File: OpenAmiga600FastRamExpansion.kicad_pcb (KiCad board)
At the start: 2 copper layers, 71.8 x 72 mm, 11 parts, among them J1 MC68000_PLCC68, P1 JTAG_CONNECTOR, P99 OSHW_LOGO, U1 ATF1502AS-10JU44, U2 74LS157, U3 HYB5118160BSJ, U4 HYB5118160BSJ, U7 74LS157

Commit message: Ready for routing!
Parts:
- removed U7: 74LS157, Package_SO:SOIC-16W_5.3x10.2mm_P1.27mm
- added C1: 100n, Capacitor_SMD:C_0805_2012Metric_Pad1.15x1.40mm_HandSolder, F.Cu at (168.4, 77.2)
- added C10: 100n, Capacitor_SMD:C_0805_2012Metric_Pad1.15x1.40mm_HandSolder, B.Cu at (150.5, 112.3)
- added C11: 100n, Capacitor_SMD:C_0805_2012Metric_Pad1.15x1.40mm_HandSolder, B.Cu at (162.2, 113.3)
- added C12: 100n, Capacitor_SMD:C_0805_2012Metric_Pad1.15x1.40mm_HandSolder, B.Cu at (173.6, 109.3)
- added C13: 100n, Capacitor_SMD:CP_Elec_5x5.8, F.Cu at (157.3, 90.8)
- added C14: 100n, Capacitor_SMD:CP_Elec_5x5.8, F.Cu at (157.3, 77.1)
- added C2: 100n, Capacitor_SMD:C_0805_2012Metric_Pad1.15x1.40mm_HandSolder, F.Cu at (165.6, 90.2)
- added C3: 100n, Capacitor_SMD:C_0805_2012Metric_Pad1.15x1.40mm_HandSolder, F.Cu at (124.0, 62.2)
- added C4: 100n, Capacitor_SMD:C_0805_2012Metric_Pad1.15x1.40mm_HandSolder, B.Cu at (133.3, 62.2)
- added C5: 100n, Capacitor_SMD:C_0805_2012Metric_Pad1.15x1.40mm_HandSolder, B.Cu at (152.4, 62.2)
- added C6: 100n, Capacitor_SMD:C_0805_2012Metric_Pad1.15x1.40mm_HandSolder, F.Cu at (124.0, 78.7)
- added C7: 100n, Capacitor_SMD:C_0805_2012Metric_Pad1.15x1.40mm_HandSolder, B.Cu at (133.3, 78.7)
- added C8: 100n, Capacitor_SMD:C_0805_2012Metric_Pad1.15x1.40mm_HandSolder, B.Cu at (152.4, 78.7)
- added C9: 100n, Capacitor_SMD:C_0805_2012Metric_Pad1.15x1.40mm_HandSolder, B.Cu at (162.3, 105.7)
- added LD1: LED, OpenAmiga600FastRamExpansion:LED_0805_HandSoldering_ModSilkS, F.Cu at (114.9, 96.8)
- added P98: SCREW_HOLE, MountingHole:MountingHole_2.5mm, F.Cu at (114.0, 102.0)
- added R4: 10k, Resistor_SMD:R_0805_2012Metric_Pad1.15x1.40mm_HandSolder, F.Cu at (114.9, 91.6)
- added U5: ATF1502AS-10JU44, Package_LCC:PLCC-44_THT-Socket, F.Cu at (163.5, 103.1)
- J1: footprint Package_LCC:PLCC-68_THT-Socket -> OpenAmiga600FastRamExpansion:PLCC-68_THT-SocketUpsideDown
- U1: value ATF1502AS-10JU44 -> 74LS157; footprint Package_LCC:PLCC-44_THT-Socket -> Package_SO:SOIC-16_3.9x9.9mm_P1.27mm
- U2: footprint Package_SO:SOIC-16W_5.3x10.2mm_P1.27mm -> Package_SO:SOIC-16_3.9x9.9mm_P1.27mm
- U3, U4: footprint OpenAmiga600FastRamExpansion:SOJ-42-Socket-LongPads -> OpenAmiga600FastRamExpansion:SOJ-42-LongPads
- moved P99 58.5 mm to (116.0, 122.8)
- moved R2 22.1 mm to (178.4, 121.8)
- moved R1 21.0 mm to (178.7, 102.5), turned to 180 degrees
- moved U1 20.4 mm to (175.3, 77.1), turned to 90 degrees
- moved J1 19.4 mm to (132.7, 93.0)
- moved U2 18.2 mm to (172.7, 90.2)
- moved U3 16.9 mm to (139.7, 62.3)
- moved U4 16.4 mm to (139.7, 78.7)
- moved R3 13.1 mm to (178.6, 105.0), turned to 180 degrees
- moved P1 12.7 mm to (177.3, 108.2)
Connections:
- U1 pad 1: /~reset -> /mux_switch
- U1 pad 10: GND -> /a12
- U1 pad 11: /d15 -> /a9
- U1 pad 12: /a23 -> /ma9
- U1 pad 13: /jtag_tms -> /a11
- U1 pad 14: /a22 -> /a10
- U1 pad 15: VCC -> GND
- U1 pad 16: /a21 -> VCC
- U1 pad 2: /~as -> /a7
- U1 pad 3: VCC -> /a14
- U1 pad 4: /ma1 -> /ma6
- U1 pad 5: /ma0 -> /a8
- U1 pad 6: /d12 -> /a13
- U1 pad 7: /jtag_tdi -> /ma7
- U1 pad 8: /d13 -> GND
- U1 pad 9: /d14 -> /ma8
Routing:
- added copper zone on B.Cu, net GND
- added copper zone on F.Cu, net GND
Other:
- outline, holes or cut-outs redrawn
- net class Default: trace_width 0.25 -> 0.2; via_dia 0.8 -> 0.6
- net class Power added: clearance 0.2, trace_width 0.5, via_dia 0.8, via_drill 0.6
- board text added: "JTAG"

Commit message: Final disposition?
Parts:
- moved C1 2.80 mm to (165.6, 77.1)
- moved U1 2.65 mm to (172.7, 77.1)
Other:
- board size 71.8 x 72 mm -> 71.7 x 72 mm

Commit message: Routing in progress...
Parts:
- removed C14: 100n, Capacitor_SMD:CP_Elec_5x5.8
- C13: value 100n -> 10u; footprint Capacitor_SMD:CP_Elec_5x5.8 -> Capacitor_THT:CP_Radial_D5.0mm_P2.00mm
- C5, C8: moved to F.Cu
- moved C13 45.6 mm to (114.3, 106.0)
- moved C5 3.05 mm to (155.4, 62.2)
- moved C8 3.05 mm to (155.4, 78.7)
- moved R2 0.49 mm to (178.6, 121.3), turned to 180 degrees
- moved C9 0.13 mm to (162.2, 105.7)
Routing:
- net /clk: track 0.00 -> 109.3 mm, vias 0 -> 2
- net /~ucas: track 0.00 -> 105.2 mm, vias 0 -> 1
- net /~reset: track 0.00 -> 104.4 mm, vias 0 -> 2
- net /a16: track 0.00 -> 90.2 mm, vias 0 -> 2
- net /d14: track 0.00 -> 80.1 mm, vias 0 -> 1
- net /a8: track 0.00 -> 72.8 mm, vias 0 -> 1
- net /ma8: track 0.00 -> 66.2 mm, vias 0 -> 2
- net /ma9: track 0.00 -> 64.7 mm, vias 0 -> 2
- net /ma7: track 0.00 -> 63.5 mm, vias 0 -> 2
- net VCC: track 0.00 -> 62.4 mm
- net /ma6: track 0.00 -> 57.7 mm, vias 0 -> 2
- net /d13: track 0.00 -> 52.9 mm, vias 0 -> 1
- net /a1: track 0.00 -> 52.8 mm
- net /r~w: track 0.00 -> 52.3 mm
- net /jtag_tms: track 0.00 -> 45.7 mm
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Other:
- outline, holes or cut-outs redrawn
- rule pad_to_mask_clearance: 0.051 -> 0

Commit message: Routing in progress... (Part II)
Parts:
- moved C10 8.73 mm to (159.1, 111.0)
- moved C7 1.02 mm to (132.3, 78.7), turned to 180 degrees
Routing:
- net /~lcas: track 17.0 -> 89.0 mm, vias 0 -> 3
- net /mux_switch: track 0.00 -> 69.1 mm, vias 0 -> 4
- net /a12: track 0.00 -> 68.7 mm, vias 0 -> 1
- net /a10: track 0.00 -> 67.7 mm, vias 0 -> 1
- net /a9: track 0.00 -> 65.9 mm, vias 0 -> 1
- net /~ras2: track 0.00 -> 65.3 mm, vias 0 -> 2
- net /a11: track 0.00 -> 64.6 mm, vias 0 -> 1
- net /a7: track 0.00 -> 57.7 mm, vias 0 -> 1
- net /a13: track 0.00 -> 56.6 mm, vias 0 -> 1
- net /a14: track 0.00 -> 55.1 mm, vias 0 -> 1
- net /a15: track 0.00 -> 49.0 mm, vias 0 -> 1
- net /d12: track 17.0 -> 65.8 mm, vias 0 -> 1
- net /a3: track 40.9 -> 85.9 mm
- net /d15: track 44.0 -> 88.5 mm, vias 0 -> 1
- net /a17: track 21.6 -> 63.8 mm, vias 0 -> 2
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
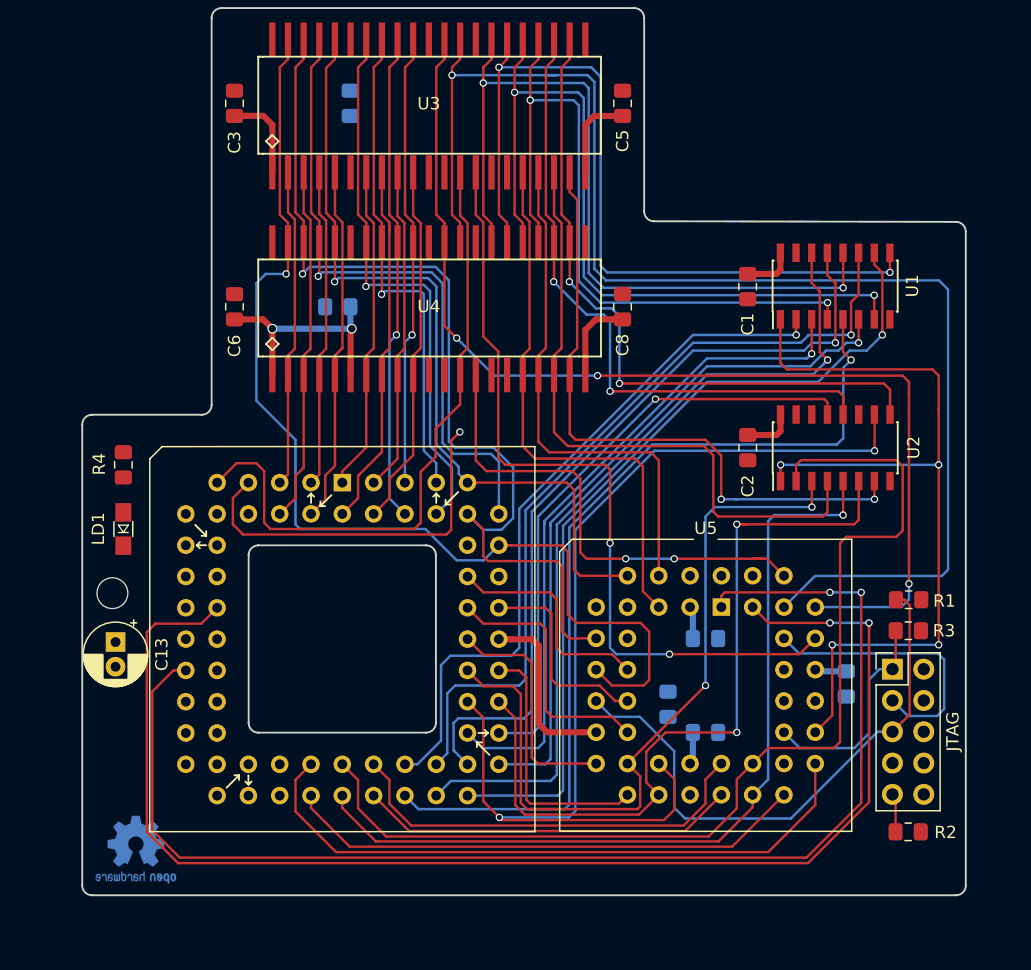
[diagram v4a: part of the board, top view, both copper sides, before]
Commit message: Routing almost done, only power TBD Also added 3D models for all components
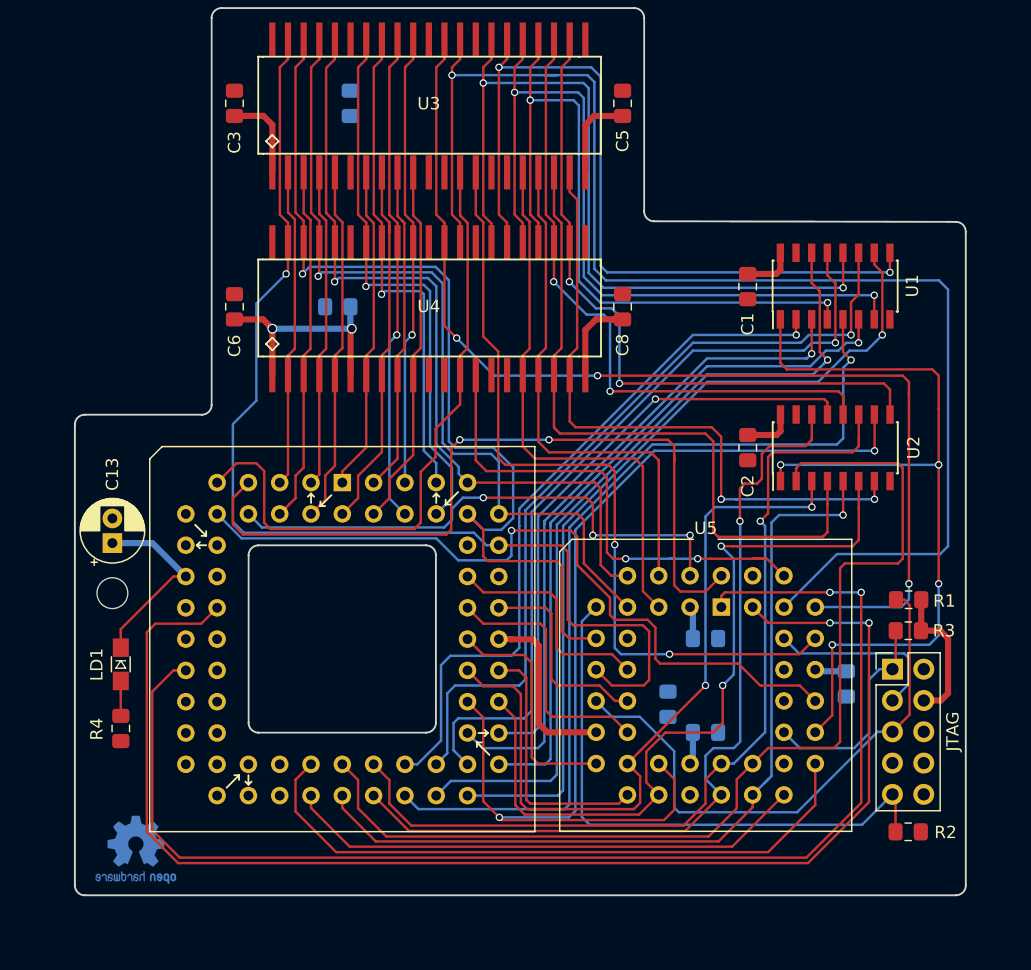
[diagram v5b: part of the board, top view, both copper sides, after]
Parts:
- moved R4 21.4 mm to (114.7, 113.0), turned to 270 degrees
- moved LD1 11.0 mm to (114.7, 107.8), turned to 270 degrees
- moved C13 8.04 mm to (114.0, 97.9), turned to 90 degrees
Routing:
- net /~lds: track 0.00 -> 61.7 mm, vias 0 -> 1
- net /jtag_tdi: track 3.14 -> 47.1 mm
- net /~as: track 0.00 -> 43.9 mm, vias 0 -> 3
- net /a6: track 30.6 -> 68.9 mm, vias 0 -> 1
- net /a5: track 34.6 -> 72.3 mm, vias 0 -> 1
- net /~uds: track 30.3 -> 63.7 mm, vias 1 -> 2
- net VCC: track 71.7 -> 99.0 mm
- net /d13: track 52.8 -> 68.4 mm
- net /jtag_tdo: track 22.7 -> 14.8 mm
- net /ma2: track 51.9 -> 55.7 mm
- net Net-(LD1-Pad2): track 0.00 -> 2.83 mm
- net /d15: track 88.5 -> 91.3 mm
- net /~ucas: track 111.6 -> 110.5 mm
- net /a17: track 63.8 -> 64.8 mm
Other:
- board size 71.7 x 72 mm -> 72.3 x 72 mm

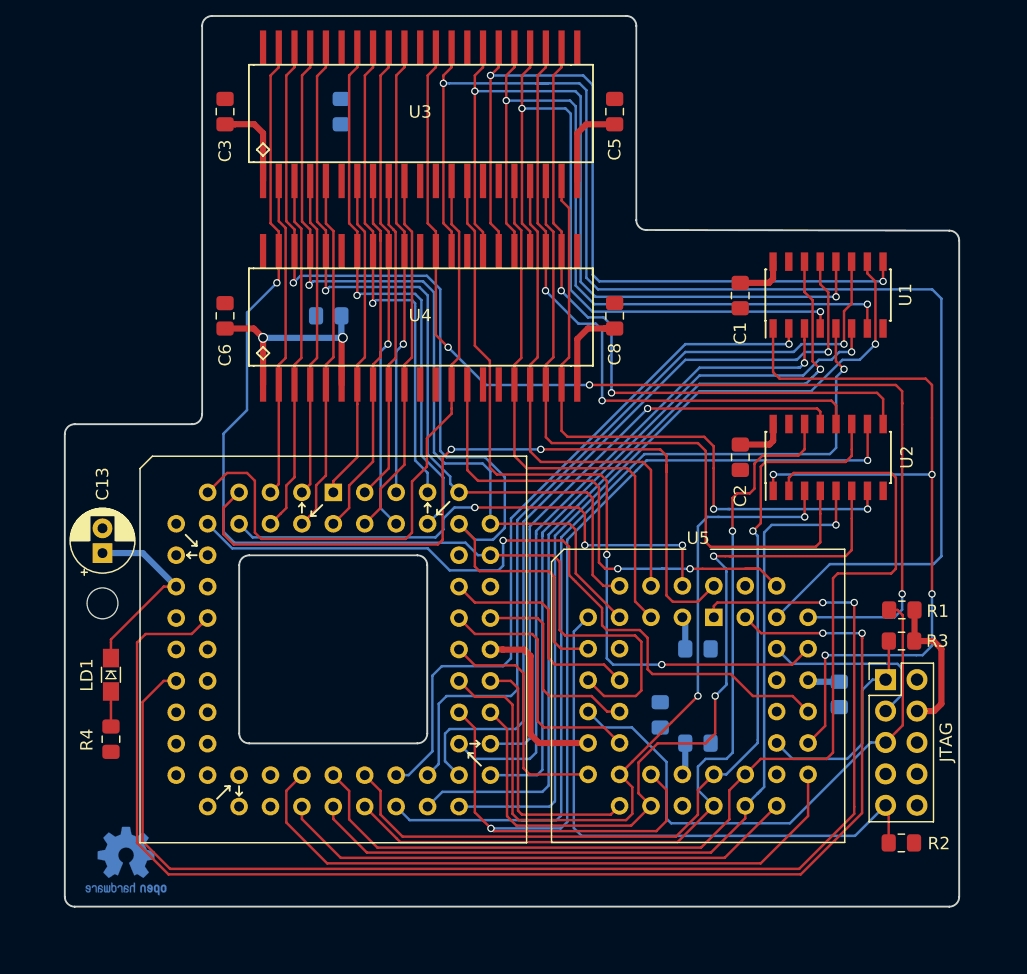
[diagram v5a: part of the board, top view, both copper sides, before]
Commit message: Routing complete Still needs some refinements
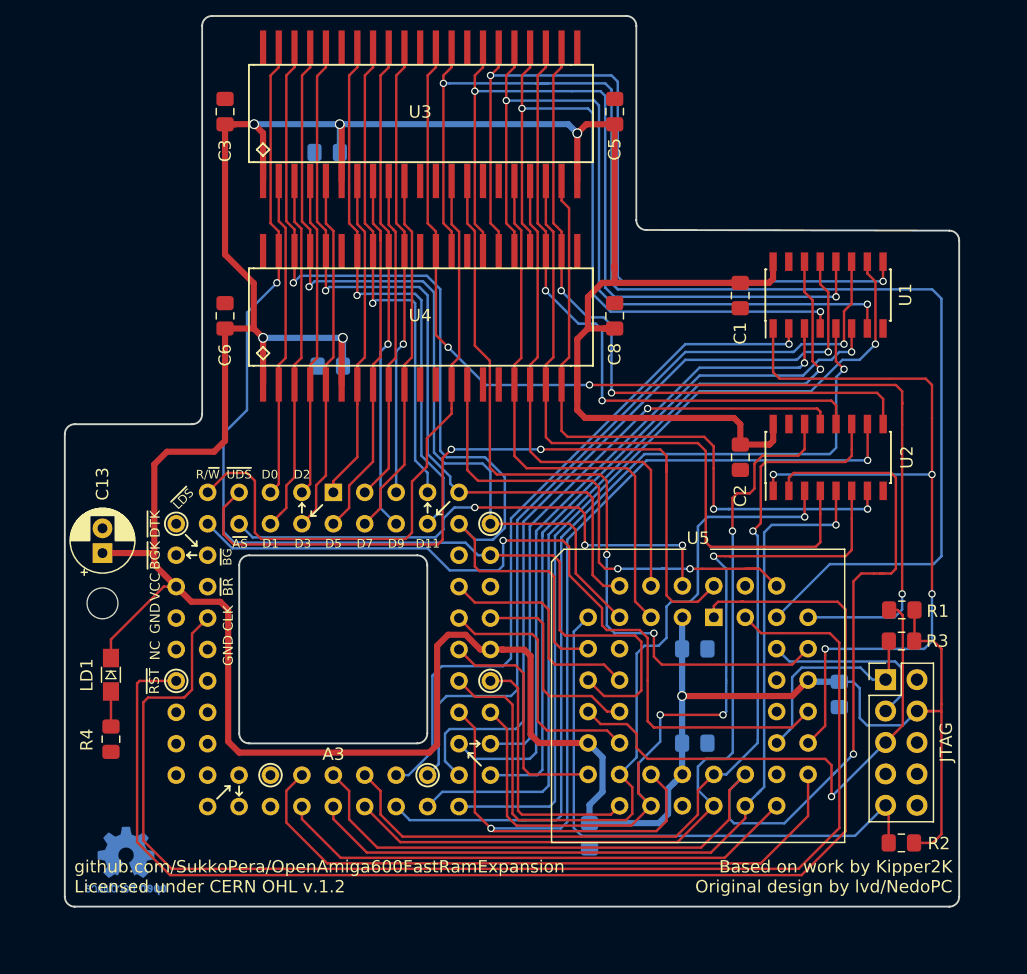
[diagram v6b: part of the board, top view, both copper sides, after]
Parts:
- moved C10 11.3 mm to (153.4, 120.8), turned to 270 degrees
- moved C7 4.07 mm to (132.5, 82.8)
- moved C4 3.49 mm to (132.2, 65.5), turned to 180 degrees
- moved C11 0.25 mm to (161.9, 113.3)
- moved C9 0.25 mm to (161.9, 105.7)
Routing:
- net VCC: track 99.0 -> 327.1 mm, vias 2 -> 6
- net /a3: track 85.6 -> 93.3 mm, vias 0 -> 1
- net /clk: track 109.3 -> 103.9 mm, vias 2 -> 0
- net /a17: track 64.8 -> 68.8 mm, vias 2 -> 3
- net /~lds: track 61.7 -> 65.2 mm
- net /jtag_tms: track 45.3 -> 43.0 mm, vias 0 -> 1
- net /~reset: track 104.4 -> 106.0 mm, vias 2 -> 0
- net /a18: track 61.4 -> 63.0 mm, vias 2 -> 1
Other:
- board text added: "A3"
- board text added: "Based on work by Kipper2K Original design by lvd/NedoPC"
- board text added: "CLK"
- board text added: "D0"
- board text added: "D1"
- board text added: "D11"
- board text added: "D2"
- board text added: "D3"
- board text added: "D5"
- board text added: "D7"
- board text added: "D9"
- board text added: "GND"
- board text added: "NC"
- board text added: "R/~W"
- board text added: "VCC"
- board text added: "github.com/SukkoPera/OpenAmiga600FastRamExpansion Licensed under CERN OHL v.1.2"
- board text added: "~AS"
- board text added: "~BG"
- board text added: "~BGK"
- board text added: "~BR"
- board text added: "~DTK"
- board text added: "~LDS"
- board text added: "~RST"
- board text added: "~UDS"

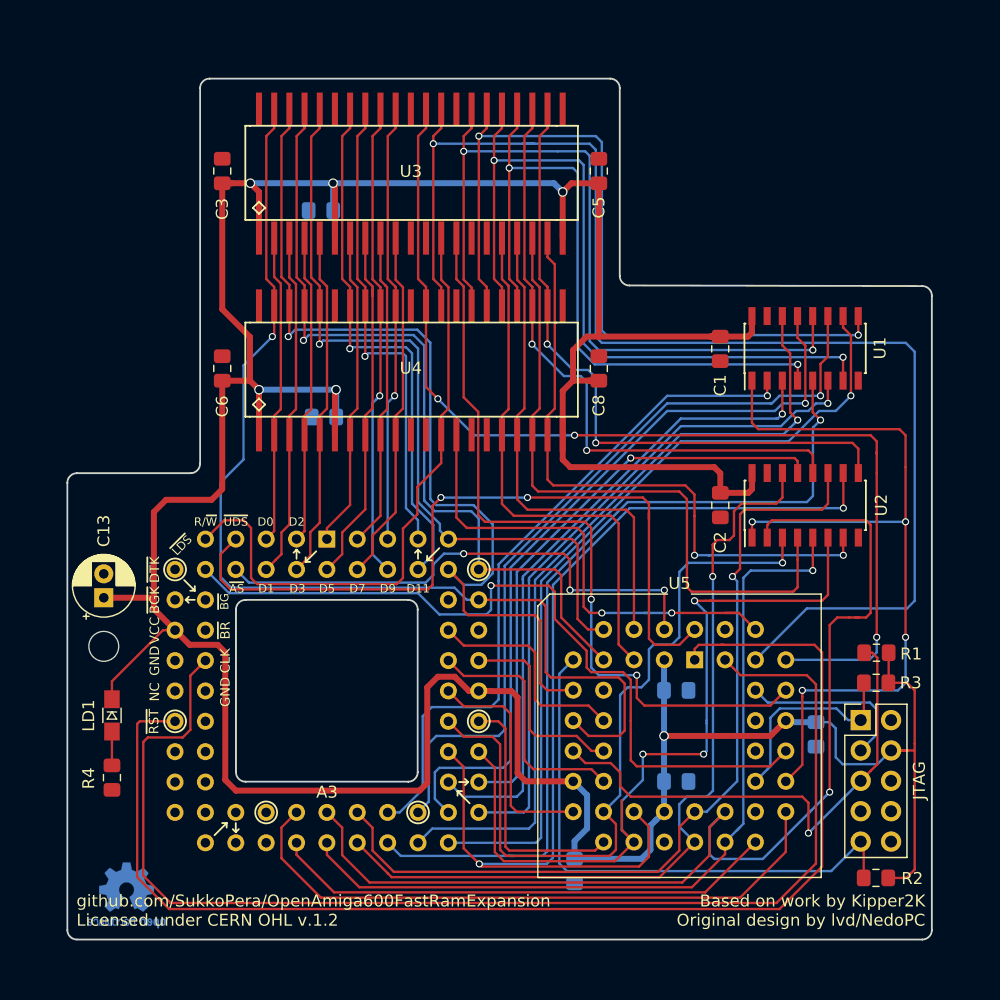
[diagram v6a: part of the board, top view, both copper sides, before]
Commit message: Stitching ground planes
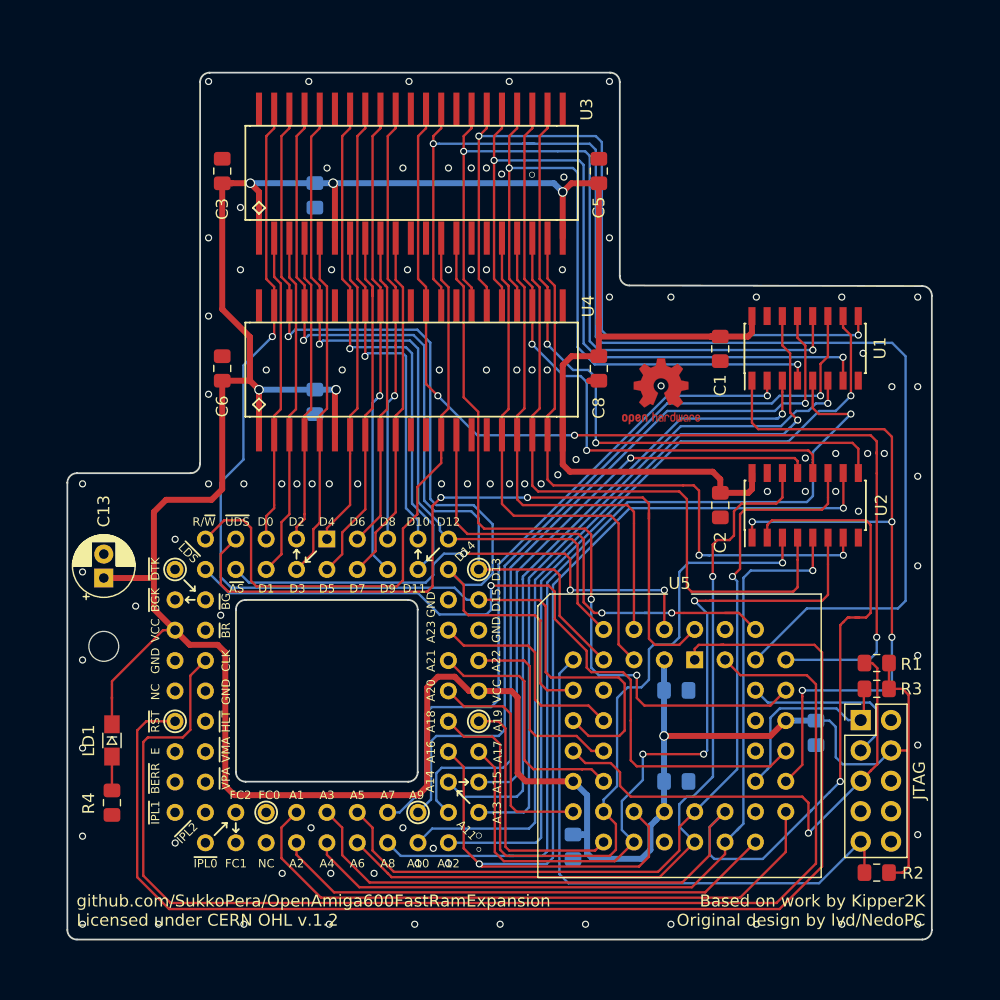
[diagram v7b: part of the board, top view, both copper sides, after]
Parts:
- P99: moved to F.Cu
- moved P99 61.5 mm to (160.7, 80.6), turned to 0 degrees
- moved LD1 2.10 mm to (114.7, 109.8)
- moved R4 2.10 mm to (114.7, 115.1)
- moved C10 2.04 mm to (153.3, 118.7)
- moved C13 1.65 mm to (114.0, 96.3)
- moved C7 1.48 mm to (131.7, 81.5), turned to 270 degrees
- moved C4 1.37 mm to (131.7, 64.3), turned to 270 degrees
- moved R1 0.86 mm to (178.7, 103.4)
- moved R3 0.51 mm to (178.7, 105.5)
- moved R2 0.45 mm to (178.7, 120.9)
- moved C12 0.13 mm to (173.6, 109.2)
- turned C8 to 270 degrees
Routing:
- net VCC: track 327.1 -> 319.6 mm
- net /a17: track 68.8 -> 65.0 mm
- net /mux_switch: track 68.7 -> 65.2 mm
- net /a8: track 72.5 -> 75.9 mm
- net /~ucas: track 110.8 -> 109.1 mm
- net /jtag_tdi: track 47.1 -> 48.1 mm
- net /jtag_tms: track 43.0 -> 42.1 mm
- net GND: track 0.00 -> 0.81 mm, vias 0 -> 99
- net /d12: track 65.6 -> 64.9 mm
- net /a6: track 68.9 -> 68.2 mm
- net /a5: track 72.3 -> 71.7 mm
- net /a3: track 93.3 -> 92.8 mm
- net /jtag_tck: track 17.3 -> 16.8 mm
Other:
- board size 72.3 x 72 mm -> 72.3 x 72.5 mm
- board text added: "A1"
- board text added: "A10"
- board text added: "A11"
- board text added: "A12"
- board text added: "A13"
- board text added: "A14"
- board text added: "A15"
- board text added: "A16"
- board text added: "A17"
- board text added: "A18"
- board text added: "A19"
- board text added: "A2"
- board text added: "A20"
- board text added: "A21"
- board text added: "A22"
- board text added: "A23"
- board text added: "A4"
- board text added: "A5"
- board text added: "A6"
- board text added: "A7"
- board text added: "A8"
- board text added: "A9"
- board text added: "D10"
- board text added: "D12"
- board text added: "D13"
- board text added: "D14"
- board text added: "D15"
- board text added: "D4"
- board text added: "D6"
- board text added: "D8"
- board text added: "E"
- board text added: "FC0"
- board text added: "FC1"
- board text added: "FC2"
- board text added: "~BERR"
- board text added: "~HLT"
- board text added: "~IPL0"
- board text added: "~IPL1"
- board text added: "~IPL2"
- board text added: "~VMA"
- board text added: "~VPA"
